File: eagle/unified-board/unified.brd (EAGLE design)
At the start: 203.2 x 101.6 mm, 101 parts, among them IC101 THAT151x, J1 eqout, J101 phantom, J103 eqout, J3 power, J601 out2, U101 lme49710, U601 LM3915N, U602 lme49710

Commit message: Duplicated input channels.
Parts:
- removed D1: (no value), SparkFun-LED:LED_5MM
- removed H10, H9: STAND-OFF, SparkFun-Hardware:STAND-OFF
- removed J1: eqout, SparkFun-Connectors:1X01NS-KIT
- removed J3: power, SparkFun-Connectors:MOLEX-1X3_LOCK
- removed R1, R2: 10r, SparkFun-Resistors:AXIAL-0.3
- removed R3: 1k5, SparkFun-Resistors:AXIAL-0.3
- added C201, C202, C301, C302, C401, C402: 47pf, mixer:CAP-KEMET-GM-2.54LS
- added C203, C204, C205, C206, C212, C213, C303, C304, C305, C306, C312, C313, C403, C404, C405, C406, C412, C413: 470pf, mixer:CAP-KEMET-GM-2.54LS
- added C207, C208, C307, C308, C407, C408: 47u/63V, mixer:CAP-PANA-5LS-6DIAM
- added C209, C210, C214, C220, C309, C310, C314, C320, C409, C410, C414, C420: 47u/25V, mixer:CAP-PANA-5LS-5DIAM
- added C211, C311, C411: 6800u/25V, mixer:CAP-PANA-5LS-12.5DIAM
- added C215, C216, C315, C316, C415, C416: 0.1uf, mixer:WIMA-MKS2-2.5X7.2
- added C217, C218, C317, C318, C417, C418: 0.015uf, mixer:WIMA-MKS2-2.5X7.2
- added C219, C319, C419: 100pf, mixer:CAP-KEMET-GM-2.54LS
- added C221, C222, C321, C322, C421, C422: 0.01uf, mixer:WIMA-MKS2-2.5X7.2
- added D201, D301, D401: RECTIFIERRB15X, mixer:SM-RECTIFIER
- added D202, D203, D302, D303, D402, D403: 1N4148, SparkFun-DiscreteSemi:DIODE-1N4148
- added D603: RED, SparkFun-LED:LED_BARGRAPH_10
- added H603, H604: STAND-OFF, SparkFun-Hardware:STAND-OFF
- added IC201, IC301, IC401: THAT151x, mosfet:DIP08-KIT
- added J105, J204, J205, J304, J305, J404, J405: eqout, SparkFun-Connectors:1X01NS-KIT
- added J201, J202, J301, J302, J401, J402: (no value), SparkFun-Connectors:1X03_NO_SILK@1
- added J203, J303, J403: phantom, SparkFun-Connectors:1X01NS-KIT
- added J206, J306, J406: (no value), SparkFun-Connectors:1X05_LONGPADS
- added J602: out2, SparkFun-Connectors:1X02_LOCK_LONGPADS
- added R201, R202, R301, R302, R401, R402: 6k8, SparkFun-Resistors:AXIAL-0.3
- added R203, R204, R303, R304, R403, R404: 10, SparkFun-Resistors:AXIAL-0.3
- added R205, R206, R305, R306, R405, R406: 4k99, SparkFun-Resistors:AXIAL-0.3
- added R207, R307, R407: 22k, SparkFun-Resistors:AXIAL-0.3
- added R208, R209, R308, R309, R408, R409: 1k2, SparkFun-Resistors:AXIAL-0.3
- added R210, R310, R410: 5, SparkFun-Resistors:AXIAL-0.3
- added R211, R212, R311, R312, R411, R412: 1k8, SparkFun-Resistors:AXIAL-0.3
- added R213, R313, R413: 12k, SparkFun-Resistors:AXIAL-0.3
- added R214, R215, R216, R314, R315, R316, R414, R415, R416: 1k, SparkFun-Resistors:AXIAL-0.3
- added R612, R613, R614: ???, SparkFun-Resistors:AXIAL-0.3
- added U201, U301, U401: lme49710, mixer:DIP08-KIT
- added VR201, VR301, VR401: 10K, mixer:ROT-SW-POT
- added VR202, VR203, VR204, VR205, VR302, VR303, VR304, VR305, VR402, VR403, VR404, VR405: 10K, mixer:ALPHA-RV24AF40-POT
- C101, C102: value 0.01uf -> 47pf; device mixer:WIMA-MKS2-2.5X7.2 -> mixer:CAP-KEMET-GM-2.54LS
- C103: value 0.015uf -> 470pf; device mixer:WIMA-MKS2-2.5X7.2 -> mixer:CAP-KEMET-GM-2.54LS
- C104, C113: value 0.1uf -> 470pf; device mixer:WIMA-MKS2-2.5X7.2 -> mixer:CAP-KEMET-GM-2.54LS
- C105: value 47u/63V -> 470pf; device mixer:CAP-PANA-5LS-6DIAM -> mixer:CAP-KEMET-GM-2.54LS
- C107: value 470pf -> 47u/63V; device mixer:CAP-KEMET-GM-2.54LS -> mixer:CAP-PANA-5LS-6DIAM
- C108: value 47pf -> 47u/63V; device mixer:CAP-KEMET-GM-2.54LS -> mixer:CAP-PANA-5LS-6DIAM
- C110: value 100pf -> 47u/25V; device mixer:CAP-KEMET-GM-2.54LS -> mixer:CAP-PANA-5LS-5DIAM
- C111: value 0.015uf -> 6800u/25V; device mixer:WIMA-MKS2-2.5X7.2 -> mixer:CAP-PANA-5LS-12.5DIAM
- C114: value 47u/63V -> 47u/25V; device mixer:CAP-PANA-5LS-6DIAM -> mixer:CAP-PANA-5LS-5DIAM
- C115: value 6800u/25V -> 0.1uf; device mixer:CAP-PANA-5LS-12.5DIAM -> mixer:WIMA-MKS2-2.5X7.2
- C116: value 470pf -> 0.1uf; device mixer:CAP-KEMET-GM-2.54LS -> mixer:WIMA-MKS2-2.5X7.2
- C117, C118: value 47u/25V -> 0.015uf; device mixer:CAP-PANA-5LS-5DIAM -> mixer:WIMA-MKS2-2.5X7.2
- C119: value 470pf -> 100pf
- C120: value 47pf -> 47u/25V; device mixer:CAP-KEMET-GM-2.54LS -> mixer:CAP-PANA-5LS-5DIAM
- C121: value 470pf -> 0.01uf; device mixer:CAP-KEMET-GM-2.54LS -> mixer:WIMA-MKS2-2.5X7.2
- C122: value 47u/25V -> 0.01uf; device mixer:CAP-PANA-5LS-5DIAM -> mixer:WIMA-MKS2-2.5X7.2
- C601: value 100pf -> 1000u/35V; device mixer:CAP-KEMET-GM-2.54LS -> mixer:CAP-PANA-5LS-12.5DIAM
- C602: value 47u/25V -> 1000u/35V; device mixer:CAP-PANA-5LS-5DIAM -> mixer:CAP-PANA-5LS-12.5DIAM
- C604: value 1000u/35V -> 47u/25V; device mixer:CAP-PANA-5LS-12.5DIAM -> mixer:CAP-PANA-5LS-5DIAM
- C606: value 1000u/35V -> 0.01uf; device mixer:CAP-PANA-5LS-12.5DIAM -> mixer:WIMA-MKS2-2.5X7.2
- C607: value 0.01uf -> 100pf; device mixer:WIMA-MKS2-2.5X7.2 -> mixer:CAP-KEMET-GM-2.54LS
- D601: value RED -> (none); device SparkFun-LED:LED_BARGRAPH_10 -> SparkFun-LED:LED_5MM
- J101: value phantom -> (none); device SparkFun-Connectors:1X01NS-KIT -> SparkFun-Connectors:1X03_NO_SILK@1
- J103: value eqout -> phantom
- J104: value (none) -> eqout; device SparkFun-Connectors:1X03_NO_SILK@1 -> SparkFun-Connectors:1X01NS-KIT
- J601: value out2 -> power; device SparkFun-Connectors:1X02_LOCK_LONGPADS -> SparkFun-Connectors:MOLEX-1X3_LOCK
- R101: value 1k8 -> 6k8
- R102: value 1k -> 6k8
- R103: value 6k8 -> 10
- R105: value 1k -> 4k99
- R106: value 1k2 -> 4k99
- R107: value 12k -> 22k
- R108: value 6k8 -> 1k2
- R111: value 10 -> 1k8
- R113: value 1k -> 12k
- R114: value 22k -> 1k
- R115, R116: value 4k99 -> 1k
- R601, R602: value ??? -> 10r
- R603: value ??? -> 1k5
- R609: value 100 -> 10k
- R610: value 47k -> 100
- R611: value 10k -> 47k
- U601: value LM3915N -> lme49710; device SparkFun-IC-Special-Function:DIL18 -> mixer:DIP08-KIT
- U602: value lme49710 -> LM3915N; device mixer:DIP08-KIT -> SparkFun-IC-Special-Function:DIL18
- VR101: device mixer:ALPHA-RV24AF40-POT -> mixer:ROT-SW-POT
- VR103: device mixer:ROT-SW-POT -> mixer:ALPHA-RV24AF40-POT
- moved C120 89.8 mm to (177.8, 6.35), turned to 180 degrees
- moved C102 84.8 mm to (190.5, 95.2), turned to 270 degrees
- moved R602 81.5 mm to (29.2, 2.54), turned to 0 degrees
- moved C103 80.3 mm to (167.6, 95.2)
- moved R601 78.6 mm to (47.0, 2.54), turned to 180 degrees
- moved R102 70.6 mm to (180.3, 88.9), turned to 0 degrees
- moved C122 70.4 mm to (177.8, 11.4), turned to 0 degrees
- moved C121 69.3 mm to (177.8, 26.7), turned to 0 degrees
- moved R603 69.3 mm to (34.3, 7.62), turned to 0 degrees
- moved C101 69.0 mm to (170.2, 95.2), turned to 270 degrees
- moved C119 69.0 mm to (185.4, 26.7)
- moved D601 68.7 mm to (38.1, 11.4)
- moved J104 67.4 mm to (185.4, 31.8), turned to 90 degrees
- moved J103 65.1 mm to (186.8, 86.3), turned to 90 degrees
- moved C117 62.2 mm to (193.0, 19.1)
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- renumbered H1 to H612, H11 to H601, H12 to H602, H2 to H611, H3 to H609, H4 to H610, H5 to H608, H6 to H607, H7 to H605, H8 to H606, J2 to J106
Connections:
- new net EQ1OUT1: C220.NEG, J205.1, J206.1
- new net EQ1OUT2: C320.NEG, J305.1, J306.1
- new net EQ1OUT3: C420.NEG, J405.1, J406.1
- new net HIGHEST: D603.20, U602.10
- new net LOWEST: D603.11, U602.1
- new net N$100: C307.NEG, R303.P$2
- new net N$101: R307.P$1, R308.P$2, R309.P$1
- new net N$102: C311.NEG, D303.A, IC301.8
- new net N$103: D302.A, IC301.1, VR301.CCW, VR301.WIP
- new net N$104: C318.P$1, VR303.CW
- new net N$105: C317.P$2, VR303.CCW
- new net N$106: R310.P$1, VR301.CW
- new net N$107: C311.POS, R310.P$2
- new net N$108: C302.P$1, J302.2
- new net N$109: C302.P$2, C305.P$2, C306.P$1
- new net N$110: C305.P$1, C309.POS, J302.3
- new net N$111: C306.P$2, C310.POS, J302.1
- new net N$112: C310.NEG, R306.P$2
- new net N$113: C309.NEG, R305.P$2
- new net N$114: D301.AC1, D302.C, IC301.2, R303.P$1, R305.P$1, R308.P$1
- new net N$115: D301.AC2, D303.C, IC301.3, R304.P$1, R306.P$1, R309.P$2
- new net N$116: C319.P$2, C320.POS, R311.P$2, R315.P$2, U301.6
- new net N$117: C414.NEG, J404.1, R412.P$1, R416.P$1
- new net N$118: C415.P$1, R411.P$1, VR402.CCW
- new net N$119: C416.P$1, R412.P$2, VR402.CW
- new net N$120: R414.P$1, VR403.WIP
- new net N$121: C415.P$2, C416.P$2, R413.P$2, VR402.WIP
- new net N$122: C418.P$2, R416.P$2
- new net N$123: C417.P$1, R415.P$1
- new net N$124: C419.P$1, R413.P$1, R414.P$2, U401.2
- new net N$125: C414.POS, IC401.6
- new net N$126: C401.P$1, J401.2
- new net N$127: C401.P$2, C403.P$2, C404.P$1
- new net N$128: C403.P$1, C407.POS, J401.3, R401.P$1
- new net N$129: C404.P$2, C408.POS, J401.1, R402.P$1
- new net N$130: C408.NEG, R404.P$2
- new net N$131: J403.1, R401.P$2, R402.P$2
- new net N$132: C407.NEG, R403.P$2
- new net N$133: R407.P$1, R408.P$2, R409.P$1
- new net N$134: C411.NEG, D403.A, IC401.8
- new net N$135: D402.A, IC401.1, VR401.CCW, VR401.WIP
- new net N$136: C418.P$1, VR403.CW
- new net N$137: C417.P$2, VR403.CCW
- new net N$138: R410.P$1, VR401.CW
- new net N$139: C411.POS, R410.P$2
- new net N$140: C402.P$1, J402.2
- new net N$141: C402.P$2, C405.P$2, C406.P$1
- new net N$142: C405.P$1, C409.POS, J402.3
- new net N$143: C406.P$2, C410.POS, J402.1
- new net N$144: C410.NEG, R406.P$2
- new net N$145: C409.NEG, R405.P$2
- new net N$146: D401.AC1, D402.C, IC401.2, R403.P$1, R405.P$1, R408.P$1
- new net N$147: D401.AC2, D403.C, IC401.3, R404.P$1, R406.P$1, R409.P$2
- new net N$148: C419.P$2, C420.POS, R411.P$2, R415.P$2, U401.6
- new net N$55: C216.P$1, R212.P$2, VR202.CW
- new net N$56: R214.P$1, VR203.WIP
- new net N$57: C215.P$2, C216.P$2, R213.P$2, VR202.WIP
- new net N$58: C218.P$2, R216.P$2
- new net N$59: C217.P$1, R215.P$1
- new net N$60: C219.P$1, R213.P$1, R214.P$2, U201.2
- new net N$61: C214.POS, IC201.6
- new net N$62: C201.P$1, J201.2
- new net N$63: C201.P$2, C203.P$2, C204.P$1
- new net N$64: C203.P$1, C207.POS, J201.3, R201.P$1
- new net N$65: C204.P$2, C208.POS, J201.1, R202.P$1
- new net N$66: C208.NEG, R204.P$2
- new net N$67: J203.1, R201.P$2, R202.P$2
- new net N$68: C207.NEG, R203.P$2
- new net N$69: R207.P$1, R208.P$2, R209.P$1
- new net N$70: C211.NEG, D203.A, IC201.8
- new net N$71: D202.A, IC201.1, VR201.CCW, VR201.WIP
- new net N$72: C218.P$1, VR203.CW
- new net N$73: C217.P$2, VR203.CCW
- new net N$74: R210.P$1, VR201.CW
- new net N$75: C211.POS, R210.P$2
- new net N$76: C202.P$1, J202.2
- new net N$77: C202.P$2, C205.P$2, C206.P$1
- new net N$78: C205.P$1, C209.POS, J202.3
- new net N$79: C206.P$2, C210.POS, J202.1
- new net N$80: C210.NEG, R206.P$2
- new net N$81: C209.NEG, R205.P$2
- new net N$82: D201.AC1, D202.C, IC201.2, R203.P$1, R205.P$1, R208.P$1
- new net N$83: D201.AC2, D203.C, IC201.3, R204.P$1, R206.P$1, R209.P$2
- new net N$84: C219.P$2, C220.POS, R211.P$2, R215.P$2, U201.6
- new net N$85: C314.NEG, J304.1, R312.P$1, R316.P$1
- new net N$86: C315.P$1, R311.P$1, VR302.CCW
- new net N$87: C316.P$1, R312.P$2, VR302.CW
- new net N$88: R314.P$1, VR303.WIP
- new net N$89: C315.P$2, C316.P$2, R313.P$2, VR302.WIP
- new net N$90: C318.P$2, R316.P$2
- new net N$91: C317.P$1, R315.P$1
- new net N$92: C319.P$1, R313.P$1, R314.P$2, U301.2
- new net N$93: C314.POS, IC301.6
- new net N$94: C301.P$1, J301.2
- new net N$95: C301.P$2, C303.P$2, C304.P$1
- new net N$96: C303.P$1, C307.POS, J301.3, R301.P$1
- new net N$97: C304.P$2, C308.POS, J301.1, R302.P$1
- new net N$98: C308.NEG, R304.P$2
- new net N$99: J303.1, R301.P$2, R302.P$2
- net 1TO1: now also J206.2, J306.2, J406.2
- net 1TO2: now also J206.3, J306.3, J406.3
- net 2TO2: now also R605.P$2; no longer R606.P$2
- net 3TO2: now also R606.P$2; no longer R607.P$2
- net 4TO2: now also R607.P$2; no longer R608.P$2
- net EQ1OUT: now also C120.NEG, J105.1; no longer C118.NEG, J103.1
- net GND: now also C112.P$2, C113.P$2, C121.P$2, C122.P$1, C212.P$2, C213.P$2, C221.P$2, C222.P$1, C312.P$2, C313.P$2, C321.P$2, C322.P$1, C412.P$2, C413.P$2, C421.P$2, C422.P$1, C601.NEG, C602.POS, C606.P$1, C607.P$2, D601.K, IC201.5, IC301.5, IC401.5, J206.4, J206.5, J306.4, J306.5, J406.4, J406.5, J602.2, R107.P$2, R207.P$2, R307.P$2, R407.P$2, R608.P$1, R611.P$2, R612.P$2, U201.3, U301.3, U401.3, U602.2, U602.4, VR204.CCW, VR205.CCW, VR304.CCW, VR305.CCW, VR404.CCW, VR405.CCW; no longer C101.P$2, C102.P$1, C106.P$2, C116.P$2, C603.P$2, C604.NEG, C606.POS, C607.P$1, D1.K, J3.2, R114.P$2, R602.P$2, R610.P$2, R611.P$1, U601.2, U601.4
- net N$1: now also C115.P$1, R111.P$1; no longer C104.P$1, R101.P$1
- net N$10: now also C118.P$1, VR103.CW; no longer C111.P$1, VR101.CW
- net N$11: now also C604.NEG, R611.P$1, U602.5; no longer C602.NEG, R610.P$1, U601.5
- net N$12: now also C604.POS, R610.P$1; no longer C602.POS, R605.P$1
- net N$13: now also R608.P$2, U601.3; no longer R611.P$2, U602.3
- net N$14: now also C115.P$2, C116.P$2, R113.P$2; no longer C104.P$2, C113.P$2, R107.P$2
- net N$15: now also C117.P$2, VR103.CCW; no longer C103.P$2, VR101.CCW
- net N$16: now also C603.P$2, R610.P$2, U601.6; no longer C601.P$2, R609.P$2, U602.6
- net N$17: now also C603.P$1, R605.P$1, R609.P$2, U601.2; no longer C601.P$1, R605.P$2, R608.P$1, U602.2
- net N$18: now also J601.3, R601.P$2; no longer J3.3, R1.P$2
- net N$19: now also C117.P$1, R115.P$1; no longer C103.P$1, R102.P$1
- net N$2: now also C116.P$1; no longer C113.P$1
- net N$20: now also C214.NEG, J204.1, R212.P$1, R216.P$1; no longer D601.11, U601.1
- net N$21: now also C111.NEG; no longer C115.NEG
- net N$22: now also C114.POS; no longer C109.POS
- net N$23: now also C101.P$1, J101.2; no longer C108.P$1, J102.2
- net N$24: now also C101.P$2, C103.P$2, C104.P$1; no longer C107.P$2, C108.P$2, C112.P$1
- net N$25: now also C103.P$1, C107.POS, J101.3, R101.P$1; no longer C105.POS, C107.P$1, J102.3, R103.P$1
- net N$26: now also C104.P$2, C108.POS, J101.1, R102.P$1; no longer C112.P$2, C114.POS, J102.1, R108.P$1
- net N$27: now also C108.NEG, R104.P$2; no longer C114.NEG, R111.P$2
- net N$28: now also J103.1, R101.P$2, R102.P$2; no longer J101.1, R103.P$2, R108.P$2
- net N$29: now also C107.NEG, R103.P$2; no longer C105.NEG, R104.P$2
- net N$3: now also C119.P$1, R113.P$1, R114.P$2; no longer C110.P$1, R105.P$2, R107.P$1
- net N$30: now also R103.P$1, R105.P$1, R108.P$1; no longer R104.P$1, R106.P$1, R115.P$1
- net N$31: now also R104.P$1, R106.P$1; no longer R111.P$1, R116.P$1
- net N$32: now also R107.P$1, R108.P$2; no longer R106.P$2, R114.P$1
- net N$33: now also VR101.CCW, VR101.WIP; no longer VR103.CCW, VR103.WIP
- net N$34: now also VR101.CW; no longer VR103.CW
- net N$35: now also C111.POS; no longer C115.POS
- net N$36: now also C102.P$1, J102.2; no longer C120.P$1, J104.2
- net N$37: now also C102.P$2, C105.P$2, C106.P$1; no longer C119.P$2, C120.P$2, C121.P$1
- net N$38: now also C105.P$1, C109.POS, J102.3; no longer C117.POS, C119.P$1, J104.3
- net N$39: now also C106.P$2, C110.POS, J102.1; no longer C121.P$2, C122.POS, J104.1
- net N$4: now also C118.P$2, R116.P$2; no longer C111.P$2, R113.P$2
- net N$40: now also C110.NEG, R106.P$2; no longer C122.NEG, R116.P$2
- net N$41: now also D603.12, U602.18; no longer D601.12, U601.18
- net N$42: now also C109.NEG, R105.P$2; no longer C117.NEG, R115.P$2
- net N$43: now also D603.13, U602.17; no longer D601.13, U601.17
- net N$44: now also D603.14, U602.16; no longer D601.14, U601.16
- net N$45: now also D603.15, U602.15; no longer D601.15, U601.15
- net N$46: now also D603.16, U602.14; no longer D601.16, U601.14
- net N$47: now also D603.17, U602.13; no longer D601.17, U601.13
- net N$48: now also D603.18, U602.12; no longer D601.18, U601.12
- net N$49: now also D603.19, U602.11; no longer D601.19, U601.11
- net N$5: now also J601.1, R602.P$2; no longer J3.1, R2.P$2
- net N$50: now also C215.P$1, R211.P$1, VR202.CCW; no longer D601.20, U601.10
- net N$51: now also R613.P$1, R614.P$2, U602.7; no longer R601.P$2, R603.P$1, U601.7
- net N$52: now also R612.P$1, R613.P$2, U602.8; no longer R602.P$1, R603.P$2, U601.8
- net N$53: now also R614.P$1, U602.6; no longer R601.P$1, U601.6
- net N$54: now also D601.A, R603.P$2; no longer D1.A, R3.P$2
- net N$6: now also C119.P$2, C120.POS, R111.P$2, R115.P$2; no longer C110.P$2, C118.POS, R101.P$2, R102.P$2
- net N$7: now also C607.P$1, J602.1; no longer C603.P$1, J601.1
- net N$8: now also R114.P$1, VR103.WIP; no longer R105.P$1, VR101.WIP
- net N$9: now also C114.NEG, J104.1, R116.P$1; no longer C109.NEG, J1.1, R113.P$1
- net VCC: now also C112.P$1, C121.P$1, C212.P$1, C221.P$1, C312.P$1, C321.P$1, C412.P$1, C421.P$1, C601.POS, D201.POS, D301.POS, D401.POS, D603.1, D603.10, D603.2, D603.3, D603.4, D603.5, D603.6, D603.7, D603.8, D603.9, IC201.7, IC301.7, IC401.7, R601.P$1, R603.P$1, U201.7, U301.7, U401.7, U601.7, U602.3; no longer C101.P$1, C106.P$1, C604.POS, D601.1, D601.10, D601.2, D601.3, D601.4, D601.5, D601.6, D601.7, D601.8, D601.9, R1.P$1, R3.P$1, U601.3, U602.7
- net VNEG: now also C113.P$1, C122.P$2, C213.P$1, C222.P$2, C313.P$1, C322.P$2, C413.P$1, C422.P$2, C602.NEG, C606.P$2, D201.NEG, D301.NEG, D401.NEG, IC201.4, IC301.4, IC401.4, R602.P$1, U201.4, U301.4, U401.4, U601.4; no longer C102.P$2, C116.P$1, C606.NEG, C607.P$2, R2.P$1, U602.4
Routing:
- net N$14: track 0.00 -> 1.53 mm

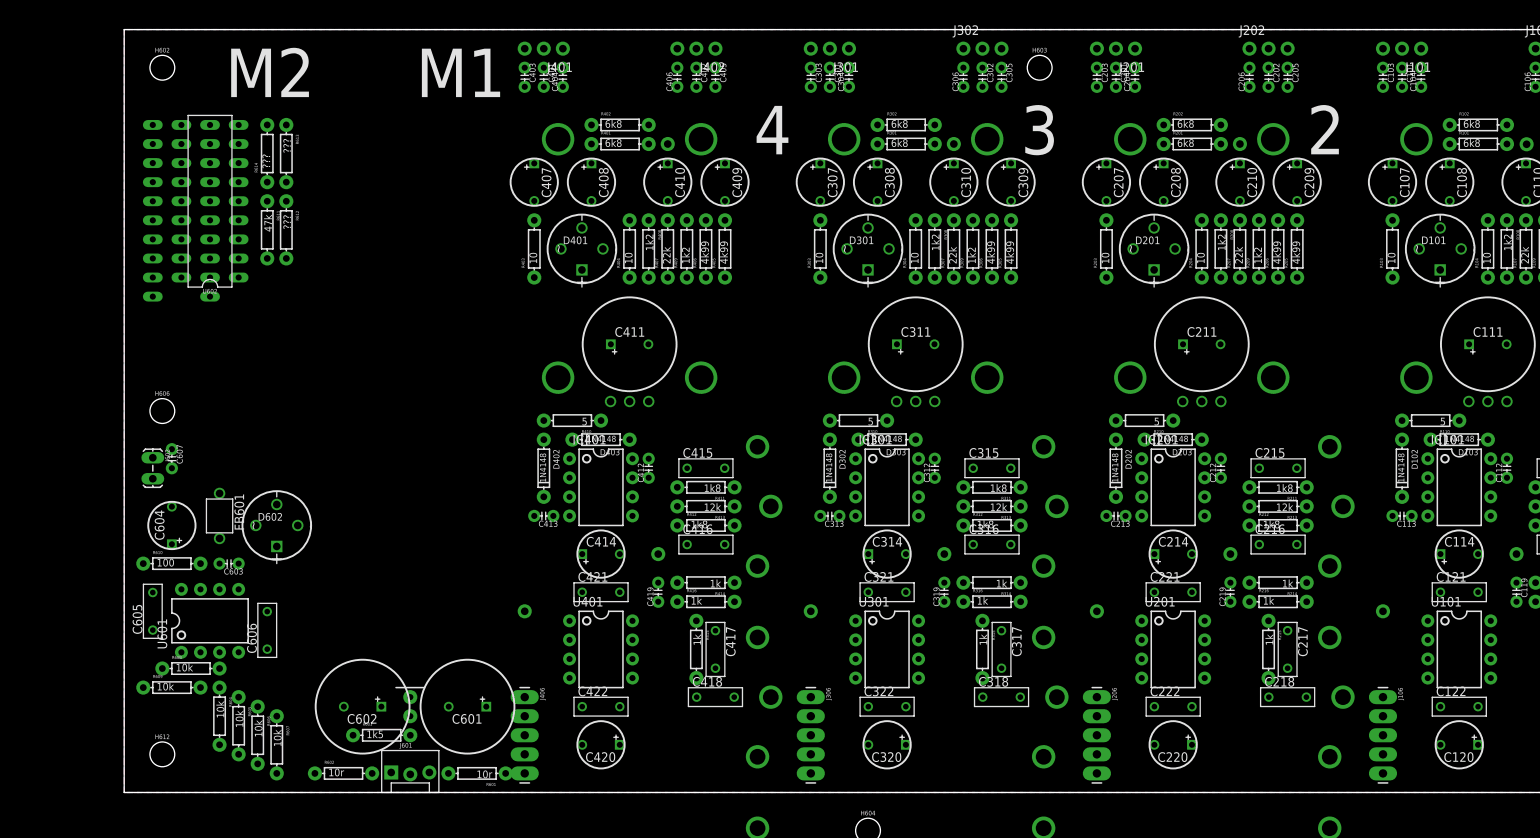
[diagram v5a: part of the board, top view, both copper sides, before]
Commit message: Assigning net classes, second summing channel.
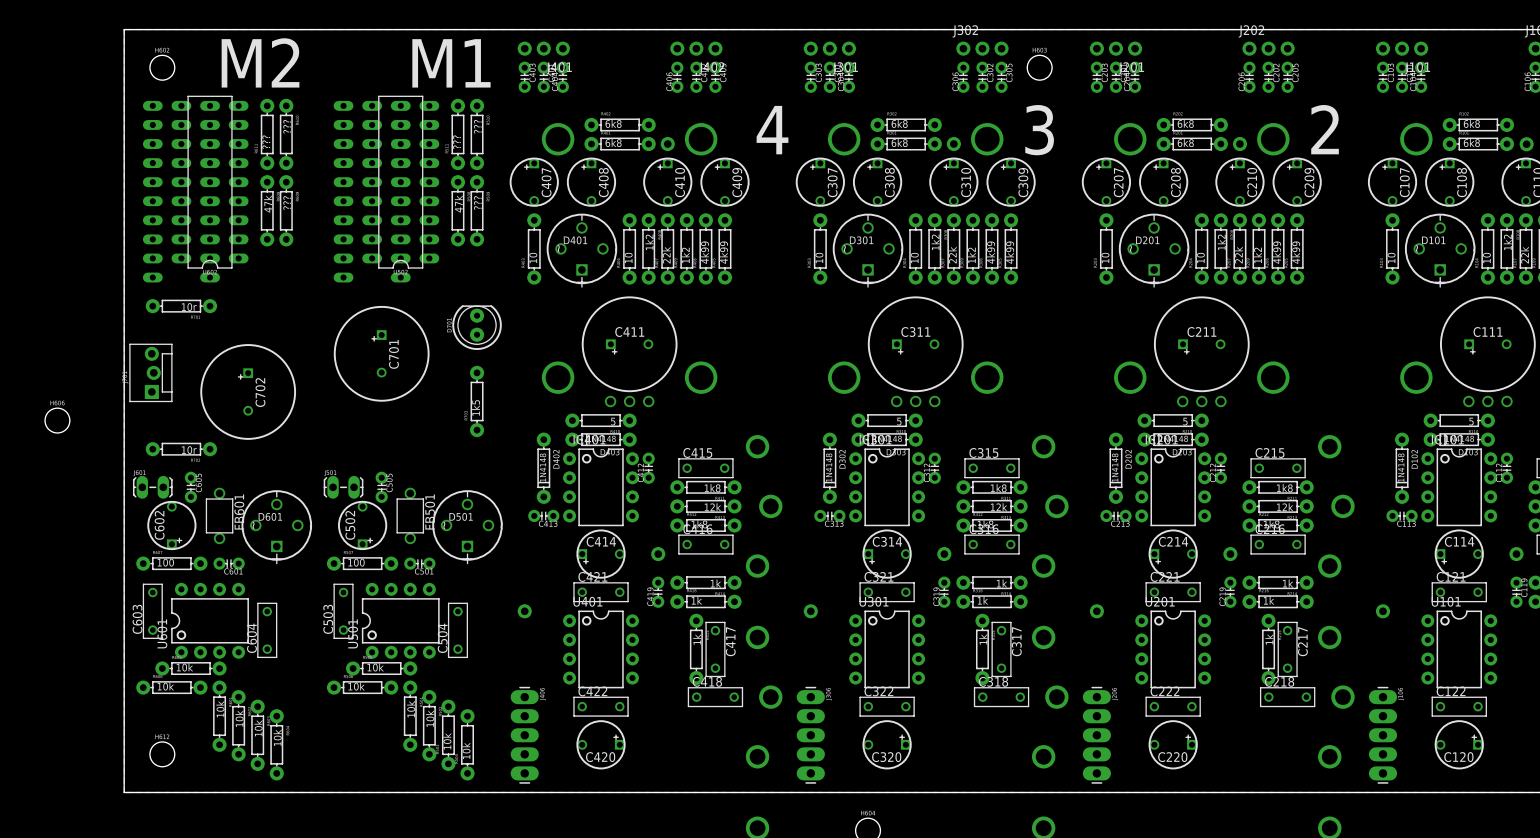
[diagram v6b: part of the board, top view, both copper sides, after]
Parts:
- removed C606: 0.01uf, mixer:WIMA-MKS2-2.5X7.2
- removed C607: 100pf, mixer:CAP-KEMET-GM-2.54LS
- removed D603: RED, SparkFun-LED:LED_BARGRAPH_10
- removed J602: out2, SparkFun-Connectors:1X02_LOCK_LONGPADS
- removed R612, R613, R614: ???, SparkFun-Resistors:AXIAL-0.3
- added C501, C505: 100pf, mixer:CAP-KEMET-GM-2.54LS
- added C502: 47u/25V, mixer:CAP-PANA-5LS-5DIAM
- added C503, C504: 0.01uf, mixer:WIMA-MKS2-2.5X7.2
- added C701, C702: 1000u/35V, mixer:CAP-PANA-5LS-12.5DIAM
- added D501: RECTIFIERRB15X, mixer:SM-RECTIFIER
- added D502: RED, SparkFun-LED:LED_BARGRAPH_10
- added D701: (no value), SparkFun-LED:LED_5MM
- added FB501: FB, mixer:BEAD
- added FRAME701: FRAME-LEDGER, SparkFun-Aesthetics:CREATIVE_COMMONS
- added J501: out2, SparkFun-Connectors:1X02_LOCK_LONGPADS
- added J701: power, SparkFun-Connectors:MOLEX-1X3_LOCK
- added R501, R502, R503, R504, R505, R506: 10k, SparkFun-Resistors:AXIAL-0.3
- added R507: 100, SparkFun-Resistors:AXIAL-0.3
- added R508: 47k, SparkFun-Resistors:AXIAL-0.3
- added R509, R510, R511: ???, SparkFun-Resistors:AXIAL-0.3
- added R701, R702: 10r, SparkFun-Resistors:AXIAL-0.3
- added R703: 1k5, SparkFun-Resistors:AXIAL-0.3
- added U501: lme49710, mixer:DIP08-KIT
- added U502: LM3915N, SparkFun-IC-Special-Function:DIL18
- C601: value 1000u/35V -> 100pf; device mixer:CAP-PANA-5LS-12.5DIAM -> mixer:CAP-KEMET-GM-2.54LS
- C602: value 1000u/35V -> 47u/25V; device mixer:CAP-PANA-5LS-12.5DIAM -> mixer:CAP-PANA-5LS-5DIAM
- C603: value 100pf -> 0.01uf; device mixer:CAP-KEMET-GM-2.54LS -> mixer:WIMA-MKS2-2.5X7.2
- C604: value 47u/25V -> 0.01uf; device mixer:CAP-PANA-5LS-5DIAM -> mixer:WIMA-MKS2-2.5X7.2
- C605: value 0.01uf -> 100pf; device mixer:WIMA-MKS2-2.5X7.2 -> mixer:CAP-KEMET-GM-2.54LS
- D601: value (none) -> RECTIFIERRB15X; device SparkFun-LED:LED_5MM -> mixer:SM-RECTIFIER
- D602: value RECTIFIERRB15X -> RED; device mixer:SM-RECTIFIER -> SparkFun-LED:LED_BARGRAPH_10
- J601: value power -> out2; device SparkFun-Connectors:MOLEX-1X3_LOCK -> SparkFun-Connectors:1X02_LOCK_LONGPADS
- R601, R602: value 10r -> 10k
- R603: value 1k5 -> 10k
- R607: value 10k -> 100
- R608: value 10k -> 47k
- R609: value 10k -> ???
- R610: value 100 -> ???
- R611: value 47k -> ???
- moved R609 65.3 mm to (21.6, 77.5), turned to 270 degrees
- moved R608 61.8 mm to (19.1, 77.5), turned to 270 degrees
- moved R610 59.1 mm to (21.6, 87.6), turned to 270 degrees
- moved J601 50.4 mm to (2.54, 40.6)
- moved D602 46.2 mm to (7.62, 80.0), flipped to the bottom, turned to 270 degrees
- moved C601 37.0 mm to (14.0, 30.5)
- moved R601 35.1 mm to (12.7, 10.2), turned to 270 degrees
- moved C602 35.0 mm to (6.35, 35.6), turned to 90 degrees
- moved D601 30.0 mm to (20.3, 35.6), flipped to the top, turned to 0 degrees
- moved R607 27.9 mm to (6.35, 30.5), turned to 0 degrees
- moved C604 18.9 mm to (19.1, 21.6)
- moved C605 17.3 mm to (8.89, 40.6), turned to 270 degrees
- moved R603 16.5 mm to (17.8, 7.62), turned to 270 degrees
- moved R602 15.3 mm to (15.2, 8.89), turned to 270 degrees
- moved H606 14.0 mm to (-8.89, 49.5)
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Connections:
- removed net N$18: J601.3, R601.P$2
- removed net N$5: J601.1, R602.P$2
- removed net N$54: D601.A, R603.P$2
- new net 2TO1: J206.2, R502.P$2
- new net 3TO1: J306.2, R503.P$2
- new net 4TO1: J406.2, R504.P$2
- new net HIGHEST1: D502.20, U502.10
- new net LOWEST1: D502.11, U502.1
- new net N$149: R505.P$2, U501.3
- new net N$150: C501.P$1, R501.P$1, R502.P$1, R503.P$1, R504.P$1, R506.P$2, U501.2
- new net N$151: C505.P$1, FB501.P$2, J501.1
- new net N$152: C502.NEG, D501.AC1, D501.AC2, FB501.P$1, R508.P$1, U502.5
- new net N$153: D502.12, U502.18
- new net N$154: D502.13, U502.17
- new net N$155: D502.14, U502.16
- new net N$156: D502.15, U502.15
- new net N$157: D502.16, U502.14
- new net N$158: D502.17, U502.13
- new net N$159: D502.18, U502.12
- new net N$160: D502.19, U502.11
- new net N$161: R510.P$1, R511.P$2, U502.7
- new net N$162: R509.P$1, R510.P$2, U502.8
- new net N$163: C501.P$2, R507.P$2, U501.6
- new net N$164: C502.POS, R506.P$1, R507.P$1
- new net N$165: R511.P$1, U502.6
- new net N$166: J701.1, R702.P$2
- new net N$167: J701.3, R701.P$2
- new net N$168: D701.A, R703.P$2
- net 1TO1: now also R501.P$2; no longer J206.2, J306.2, J406.2
- net 1TO2: now also R601.P$2; no longer J206.3, J306.3, J406.3, R604.P$2
- net 2TO2: now also J206.3, R602.P$2; no longer R605.P$2
- net 3TO2: now also J306.3, R603.P$2; no longer R606.P$2
- net 4TO2: now also J406.3, R604.P$2; no longer R607.P$2
- net GND: now also C503.P$2, C504.P$1, C505.P$2, C603.P$2, C604.P$1, C701.NEG, C702.POS, D701.K, J501.2, J701.2, R505.P$1, R508.P$2, R509.P$2, R605.P$1, R608.P$2, R609.P$2, U502.2, U502.4; no longer C601.NEG, C602.POS, C606.P$1, C607.P$2, D601.K, J602.2, R608.P$1, R611.P$2, R612.P$2
- net HIGHEST: now also D602.20; no longer D603.20
- net LOWEST: now also D602.11; no longer D603.11
- net N$11: now also C602.NEG, D601.AC1, D601.AC2, R608.P$1; no longer C604.NEG, D602.AC1, D602.AC2, R611.P$1
- net N$12: now also C602.POS, R606.P$1, R607.P$1; no longer C604.POS, R609.P$1, R610.P$1
- net N$13: now also R605.P$2; no longer R608.P$2
- net N$16: now also C601.P$2, R607.P$2; no longer C603.P$2, R610.P$2
- net N$17: now also C601.P$1, R601.P$1, R602.P$1, R603.P$1, R606.P$2; no longer C603.P$1, R605.P$1, R606.P$1, R607.P$1, R609.P$2
- net N$41: now also D602.12; no longer D603.12
- net N$43: now also D602.13; no longer D603.13
- net N$44: now also D602.14; no longer D603.14
- net N$45: now also D602.15; no longer D603.15
- net N$46: now also D602.16; no longer D603.16
- net N$47: now also D602.17; no longer D603.17
- net N$48: now also D602.18; no longer D603.18
- net N$49: now also D602.19; no longer D603.19
- net N$51: now also R610.P$1, R611.P$2; no longer R613.P$1, R614.P$2
- net N$52: now also R609.P$1, R610.P$2; no longer R612.P$1, R613.P$2
- net N$53: now also R611.P$1; no longer R614.P$1
- net N$7: now also C605.P$1, J601.1; no longer C607.P$1, J602.1
- net VCC: now also C503.P$1, C603.P$1, C701.POS, D501.POS, D502.1, D502.10, D502.2, D502.3, D502.4, D502.5, D502.6, D502.7, D502.8, D502.9, D601.POS, D602.1, D602.10, D602.2, D602.3, D602.4, D602.5, D602.6, D602.7, D602.8, D602.9, R701.P$1, R703.P$1, U501.7, U502.3; no longer C601.POS, C605.P$1, D602.POS, D603.1, D603.10, D603.2, D603.3, D603.4, D603.5, D603.6, D603.7, D603.8, D603.9, R601.P$1, R603.P$1
- net VNEG: now also C504.P$2, C604.P$2, C702.NEG, D501.NEG, D601.NEG, R702.P$1, U501.4; no longer C602.NEG, C606.P$2, D602.NEG, R602.P$1
